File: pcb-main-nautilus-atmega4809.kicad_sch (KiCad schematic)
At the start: 0 parts

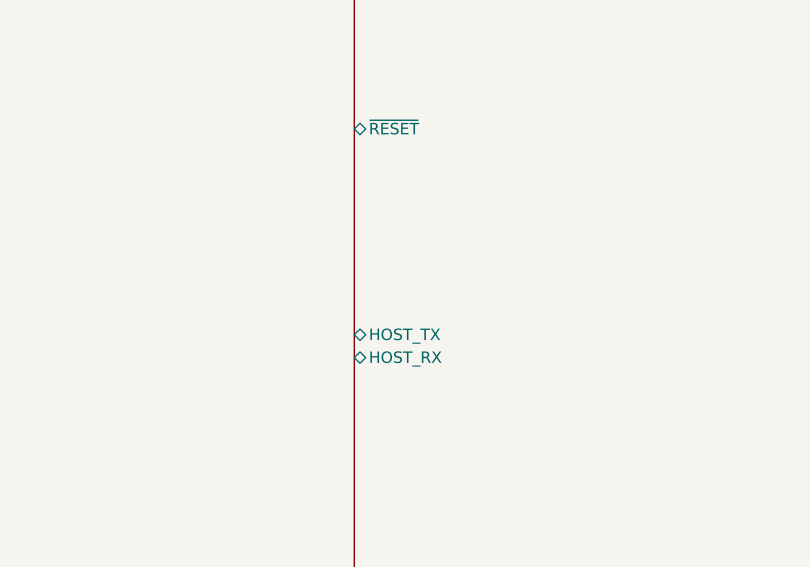
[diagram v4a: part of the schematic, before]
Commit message: Improve MCU sheet flow
Supports #2.
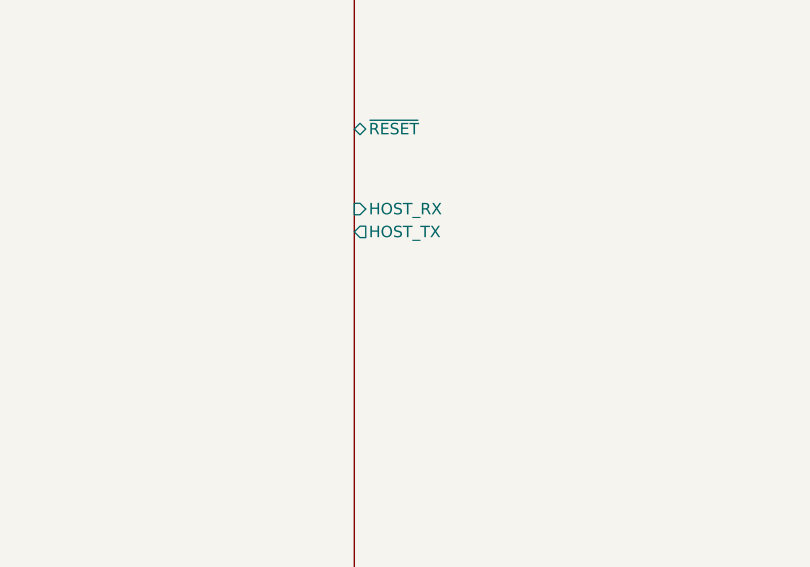
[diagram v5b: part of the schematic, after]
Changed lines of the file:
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@@
       (effects (font (size 1.27 1.27)) (justify right))
-    )
-    (pin "HOST_TX" bidirectional (at 147.32 109.22 180)
-      (effects (font (size 1.27 1.27)) (justify left))
-    )
-    (pin "HOST_RX" bidirectional (at 147.32 111.76 180)
-      (effects (font (size 1.27 1.27)) (justify left))
     )
     (pin "D8" bidirectional (at 224.79 72.39 0)
@@
     (pin "D19{slash}A5{slash}SCL" bidirectional (at 224.79 105.41 0)
       (effects (font (size 1.27 1.27)) (justify right))
+    )
+    (pin "HOST_RX" input (at 147.32 95.25 180)
+      (effects (font (size 1.27 1.27)) (justify left))
+    )
+    (pin "HOST_TX" output (at 147.32 97.79 180)
+      (effects (font (size 1.27 1.27)) (justify left))
     )
   )
@@
       (reference "D4") (unit 1) (value "GREEN") (footprint "LED_SMD:LED_0603_1608Metric_Pad1.05x0.95mm_HandSolder")
     )
+    (path "/535baf57-8641-4121-897f-4706b098c129/98ffd9eb-6a42-40ba-917a-cfeb9ee5591d"
+      (reference "D5") (unit 1) (value "YELLOW") (footprint "LED_SMD:LED_0603_1608Metric_Pad1.05x0.95mm_HandSolder")
+    )
+    (path "/535baf57-8641-4121-897f-4706b098c129/bc5c465a-4408-47a8-b403-b778f9832a23"
+      (reference "D6") (unit 1) (value "YELLOW") (footprint "LED_SMD:LED_0603_1608Metric_Pad1.05x0.95mm_HandSolder")
+    )
     (path "/535baf57-8641-4121-897f-4706b098c129/ad030bfa-9ff6-4a09-96d0-99902cfc5324"
-      (reference "D5") (unit 1) (value "RED") (footprint "LED_SMD:LED_0603_1608Metric_Pad1.05x0.95mm_HandSolder")
-    )
-    (path "/535baf57-8641-4121-897f-4706b098c129/98ffd9eb-6a42-40ba-917a-cfeb9ee5591d"
-      (reference "D6") (unit 1) (value "YELLOW") (footprint "LED_SMD:LED_0603_1608Metric_Pad1.05x0.95mm_HandSolder")
-    )
-    (path "/535baf57-8641-4121-897f-4706b098c129/bc5c465a-4408-47a8-b403-b778f9832a23"
-      (reference "D7") (unit 1) (value "YELLOW") (footprint "LED_SMD:LED_0603_1608Metric_Pad1.05x0.95mm_HandSolder")
+      (reference "D7") (unit 1) (value "RED") (footprint "LED_SMD:LED_0603_1608Metric_Pad1.05x0.95mm_HandSolder")
     )
     (path "/9563730f-8d1a-4fdb-af84-834004e725da/e8c125a0-c891-462e-9bd4-251e59b83fd3"
@@
       (reference "R12") (unit 1) (value "330/0.1W") (footprint "Resistor_SMD:R_0603_1608Metric_Pad0.98x0.95mm_HandSolder")
     )
+    (path "/535baf57-8641-4121-897f-4706b098c129/9c3a808c-58c6-4d33-9871-be9c5e46994f"
+      (reference "R13") (unit 1) (value "330/0.1W") (footprint "Resistor_SMD:R_0603_1608Metric_Pad0.98x0.95mm_HandSolder")
+    )
+    (path "/535baf57-8641-4121-897f-4706b098c129/b7c1a3dd-bee9-453f-a568-216b24a2bcec"
+      (reference "R14") (unit 1) (value "330/0.1W") (footprint "Resistor_SMD:R_0603_1608Metric_Pad0.98x0.95mm_HandSolder")
+    )
     (path "/535baf57-8641-4121-897f-4706b098c129/1c645e79-eee2-445a-97c6-a2127b2429d2"
-      (reference "R13") (unit 1) (value "330/0.1W") (footprint "Resistor_SMD:R_0603_1608Metric_Pad0.98x0.95mm_HandSolder")
-    )
-    (path "/535baf57-8641-4121-897f-4706b098c129/9c3a808c-58c6-4d33-9871-be9c5e46994f"
-      (reference "R14") (unit 1) (value "330/0.1W") (footprint "Resistor_SMD:R_0603_1608Metric_Pad0.98x0.95mm_HandSolder")
-    )
-    (path "/535baf57-8641-4121-897f-4706b098c129/b7c1a3dd-bee9-453f-a568-216b24a2bcec"
       (reference "R15") (unit 1) (value "330/0.1W") (footprint "Resistor_SMD:R_0603_1608Metric_Pad0.98x0.95mm_HandSolder")
     )

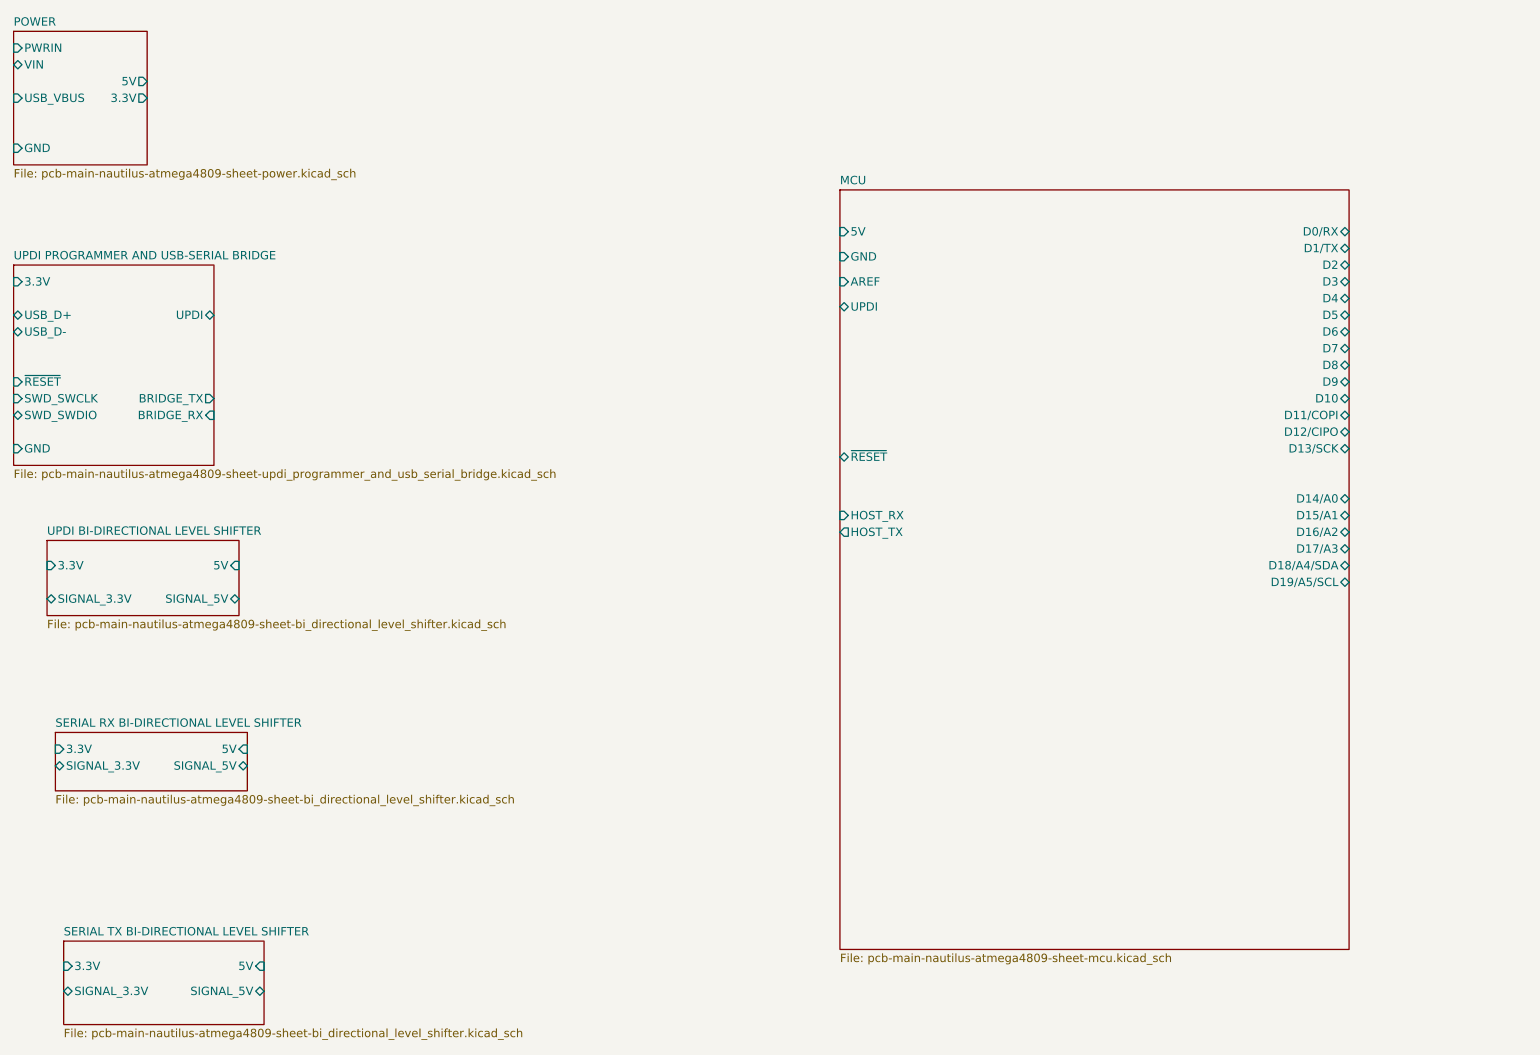
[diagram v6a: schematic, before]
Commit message: Connect root sheet
Supports #2.
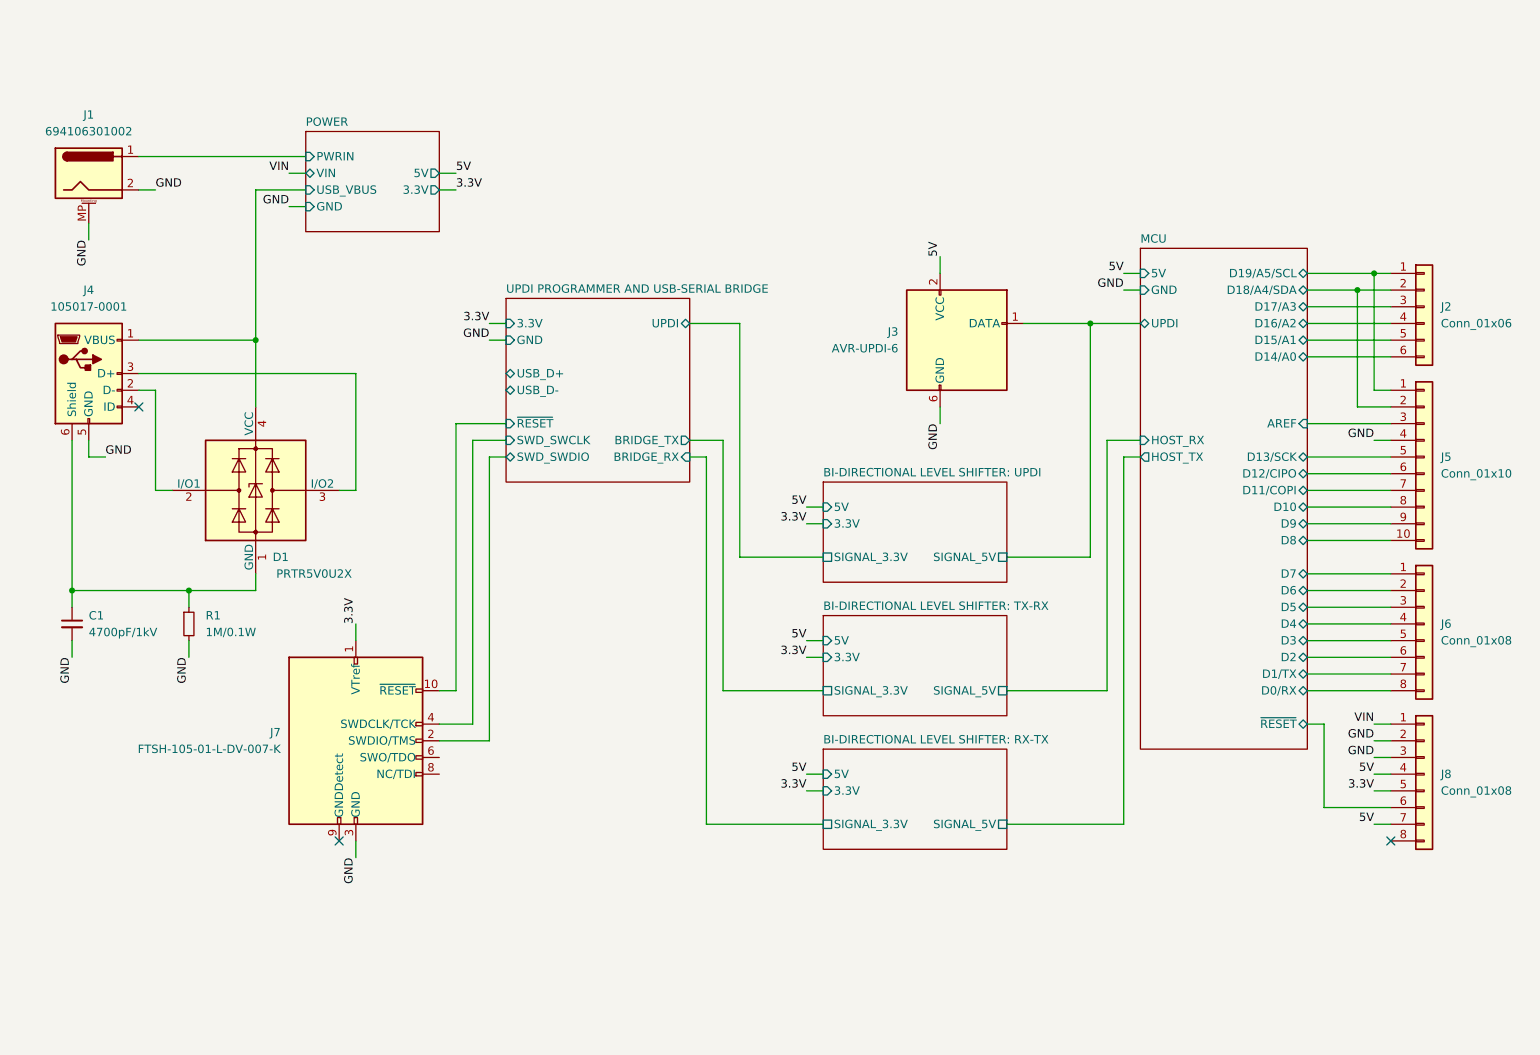
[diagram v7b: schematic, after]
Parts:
- added C1: 4700pF/1kV, Capacitor_SMD:C_0805_2012Metric_Pad1.18x1.45mm_HandSolder, symbol Device:C_Small
- added D1: PRTR5V0U2X, Package_TO_SOT_SMD:SOT-143, symbol Power_Protection:PRTR5V0U2X
- added J1: 694106301002, Connector_BarrelJack:BarrelJack_Wuerth_6941xx301002, symbol Connector:Barrel_Jack_MountingPin
- added J2: Conn_01x06, Connector_PinHeader_2.54mm:PinHeader_1x06_P2.54mm_Vertical, symbol Connector_Generic:Conn_01x06
- added J3: AVR-UPDI-6, Connector_PinHeader_2.54mm:PinHeader_2x03_P2.54mm_Vertical, symbol Connector:AVR-UPDI-6
- added J4: 105017-0001, Connector_USB:USB_Micro-B_Molex-105017-0001, symbol Connector:USB_B_Micro
- added J5: Conn_01x10, Connector_PinHeader_2.54mm:PinHeader_1x10_P2.54mm_Vertical, symbol Connector_Generic:Conn_01x10
- added J6, J8: Conn_01x08, Connector_PinHeader_2.54mm:PinHeader_1x08_P2.54mm_Vertical, symbol Connector_Generic:Conn_01x08
- added J7: FTSH-105-01-L-DV-007-K, Connector_PinSocket_1.27mm:PinSocket_2x05_P1.27mm_Vertical_SMD, symbol Connector:Conn_ARM_JTAG_SWD_10
- added R1: 1M/0.1W, Resistor_SMD:R_0603_1608Metric_Pad0.98x0.95mm_HandSolder, symbol Device:R_Small
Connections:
- net MCU/AREF: now also J5.3 (Pin_3)
- net MCU/D0/RX: now also J6.8 (Pin_8)
- net MCU/D10: now also J5.8 (Pin_8)
- net MCU/D11/COPI: now also J5.7 (Pin_7)
- net MCU/D12/CIPO: now also J5.6 (Pin_6)
- net MCU/D13/SCK: now also J5.5 (Pin_5)
- net MCU/D14/A0: now also J2.6 (Pin_6)
- net MCU/D15/A1: now also J2.5 (Pin_5)
- net MCU/D16/A2: now also J2.4 (Pin_4)
- net MCU/D17/A3: now also J2.3 (Pin_3)
- net MCU/D18/A4/SDA: now also J2.2 (Pin_2), J5.2 (Pin_2)
- net MCU/D19/A5/SCL: now also J2.1 (Pin_1), J5.1 (Pin_1)
- net MCU/D1/TX: now also J6.7 (Pin_7)
- net MCU/D2: now also J6.6 (Pin_6)
- net MCU/D3: now also J6.5 (Pin_5)
- net MCU/D4: now also J6.4 (Pin_4)
- net MCU/D5: now also J6.3 (Pin_3)
- net MCU/D6: now also J6.2 (Pin_2)
- net MCU/D7: now also J6.1 (Pin_1)
- net MCU/D8: now also J5.10 (Pin_10)
- net MCU/D9: now also J5.9 (Pin_9)
- net MCU/~{RESET}: now also J8.6 (Pin_6)
- net POWER/PWRIN: now also J1.1
- net POWER/USB_VBUS: now also D1.4 (VCC), J4.1 (VBUS)
- net BI-DIRECTIONAL LEVEL SHIFTER: UPDI/SIGNAL_5V: now also J3.1 (DATA)
- net UPDI PROGRAMMER AND USB-SERIAL BRIDGE/SWD_SWCLK: now also J7.4 (SWDCLK/TCK)
- net UPDI PROGRAMMER AND USB-SERIAL BRIDGE/SWD_SWDIO: now also J7.2 (SWDIO/TMS)
- net UPDI PROGRAMMER AND USB-SERIAL BRIDGE/~{RESET}: now also J7.10 (~{RESET})
- new net: C1.1, D1.1 (GND), J4.6 (Shield), R1.1
- new net: D1.2 (I/O1), J4.2 (D-)
- new net: D1.3 (I/O2), J4.3 (D+)
- new net 3.3V: J7.1 (VTref), J8.5 (Pin_5)
- new net 5V: J3.2 (VCC), J8.4 (Pin_4), J8.7 (Pin_7)
- new net GND: C1.2, J1.2, J1.MP (MountPin), J3.6 (GND), J4.5 (GND), J5.4 (Pin_4), J7.3 (GND), J7.5 (GND), J8.2 (Pin_2), J8.3 (Pin_3), R1.2
- new net VIN: J8.1 (Pin_1)
- no-connect marks 0 -> 3
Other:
- sheet SERIAL RX BI-DIRECTIONAL LEVEL SHIFTER renamed BI-DIRECTIONAL LEVEL SHIFTER: TX-RX
- sheet SERIAL TX BI-DIRECTIONAL LEVEL SHIFTER renamed BI-DIRECTIONAL LEVEL SHIFTER: RX-TX
- sheet UPDI BI-DIRECTIONAL LEVEL SHIFTER renamed BI-DIRECTIONAL LEVEL SHIFTER: UPDI

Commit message: Nest level shifter sheets under UPDI programmer and bridge sheet
Supports #2.
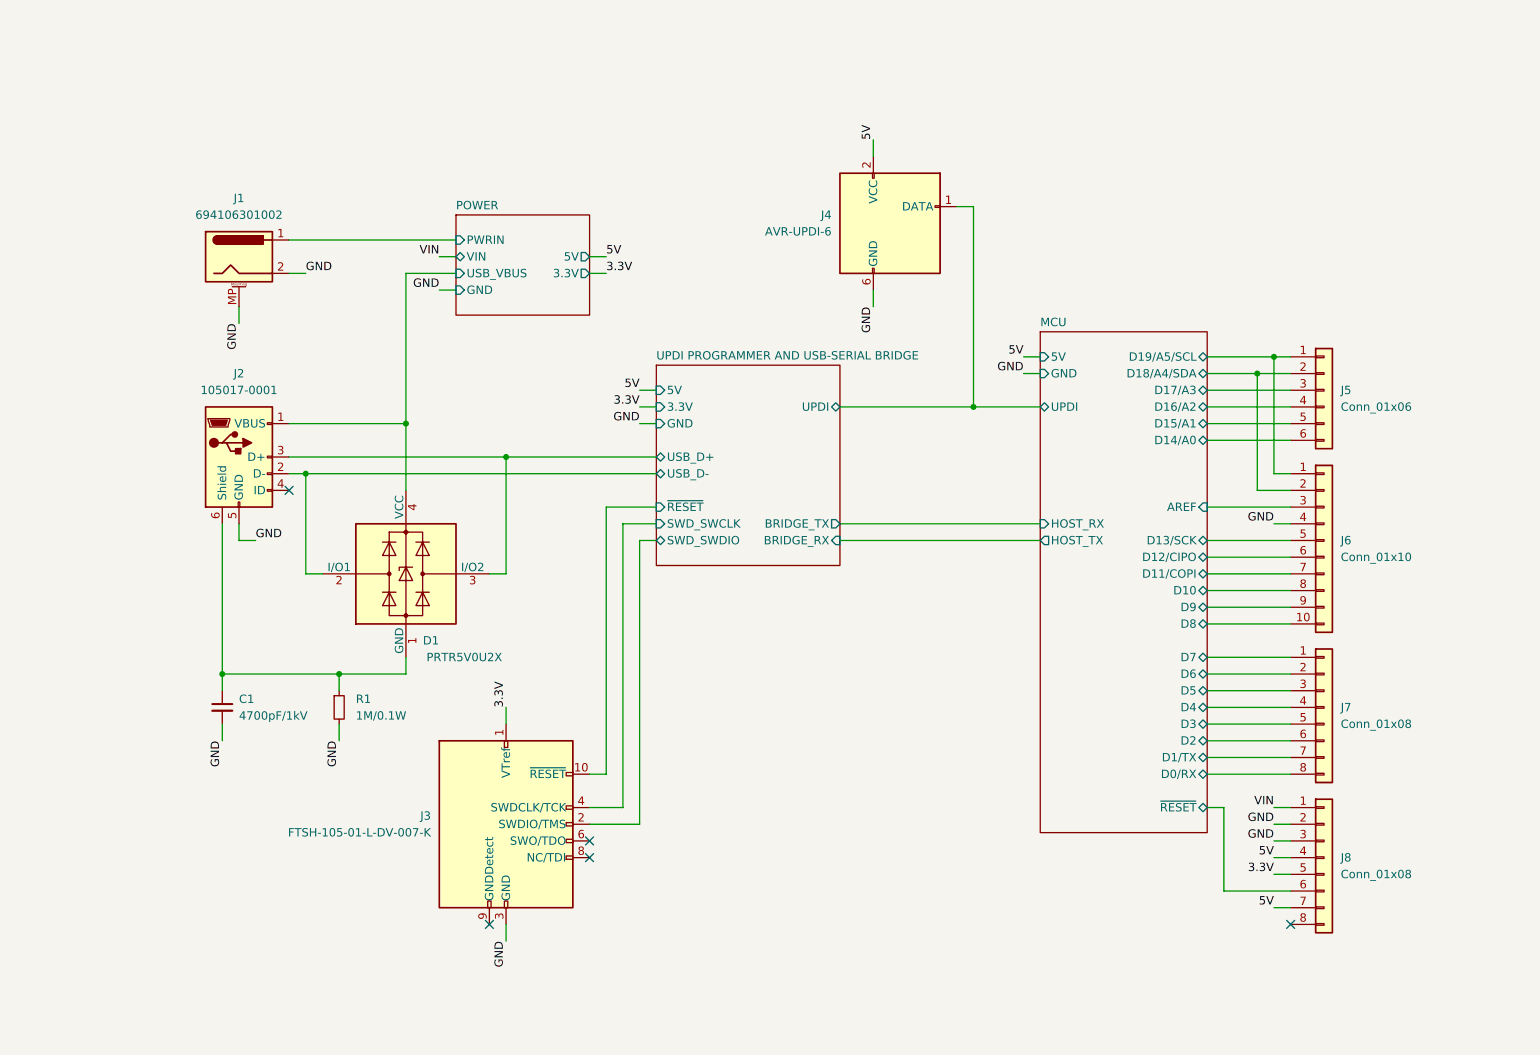
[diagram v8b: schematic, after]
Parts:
- renumbered J4 to J2, J7 to J3, J3 to J4, J2 to J5, J5 to J6, J6 to J7
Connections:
- net UPDI PROGRAMMER AND USB-SERIAL BRIDGE/USB_D+: now also D1.3 (I/O2), J2.3 (D+)
- net UPDI PROGRAMMER AND USB-SERIAL BRIDGE/USB_D-: now also D1.2 (I/O1), J2.2 (D-)
- net BI-DIRECTIONAL LEVEL SHIFTER: UPDI/SIGNAL_5V renamed MCU/UPDI
- no-connect marks 3 -> 5
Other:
- removed sheet BI-DIRECTIONAL LEVEL SHIFTER: RX-TX
- removed sheet BI-DIRECTIONAL LEVEL SHIFTER: TX-RX
- removed sheet BI-DIRECTIONAL LEVEL SHIFTER: UPDI
- sheet UPDI PROGRAMMER AND USB-SERIAL BRIDGE ports: added 5V; removed none
- moved on the sheet: C1, D1, J1, J2, J3, J4, J5, J6, J7, J8, R1
